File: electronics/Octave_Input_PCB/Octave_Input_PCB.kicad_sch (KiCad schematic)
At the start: 38 parts, among them SW1 SW_Hot_Swap_Socket, SW10 SW_Hot_Swap_Socket, SW11 SW_Hot_Swap_Socket, SW12 SW_Hot_Swap_Socket, SW13 SW_Hot_Swap_Socket, SW14 Alps_Alpine_RKJXV1224, SW15 Bourns_PEC12R-4xxxF-Sxxx, SW2 SW_Hot_Swap_Socket, SW3 SW_Hot_Swap_Socket, SW4 SW_Hot_Swap_Socket, SW5 SW_Hot_Swap_Socket, SW6 SW_Hot_Swap_Socket, SW7 SW_Hot_Swap_Socket, SW8 SW_Hot_Swap_Socket, SW9 SW_Hot_Swap_Socket, U1 Adafruit_QT_Py_RP2040, U2 Raspberry_Pi_RP2040

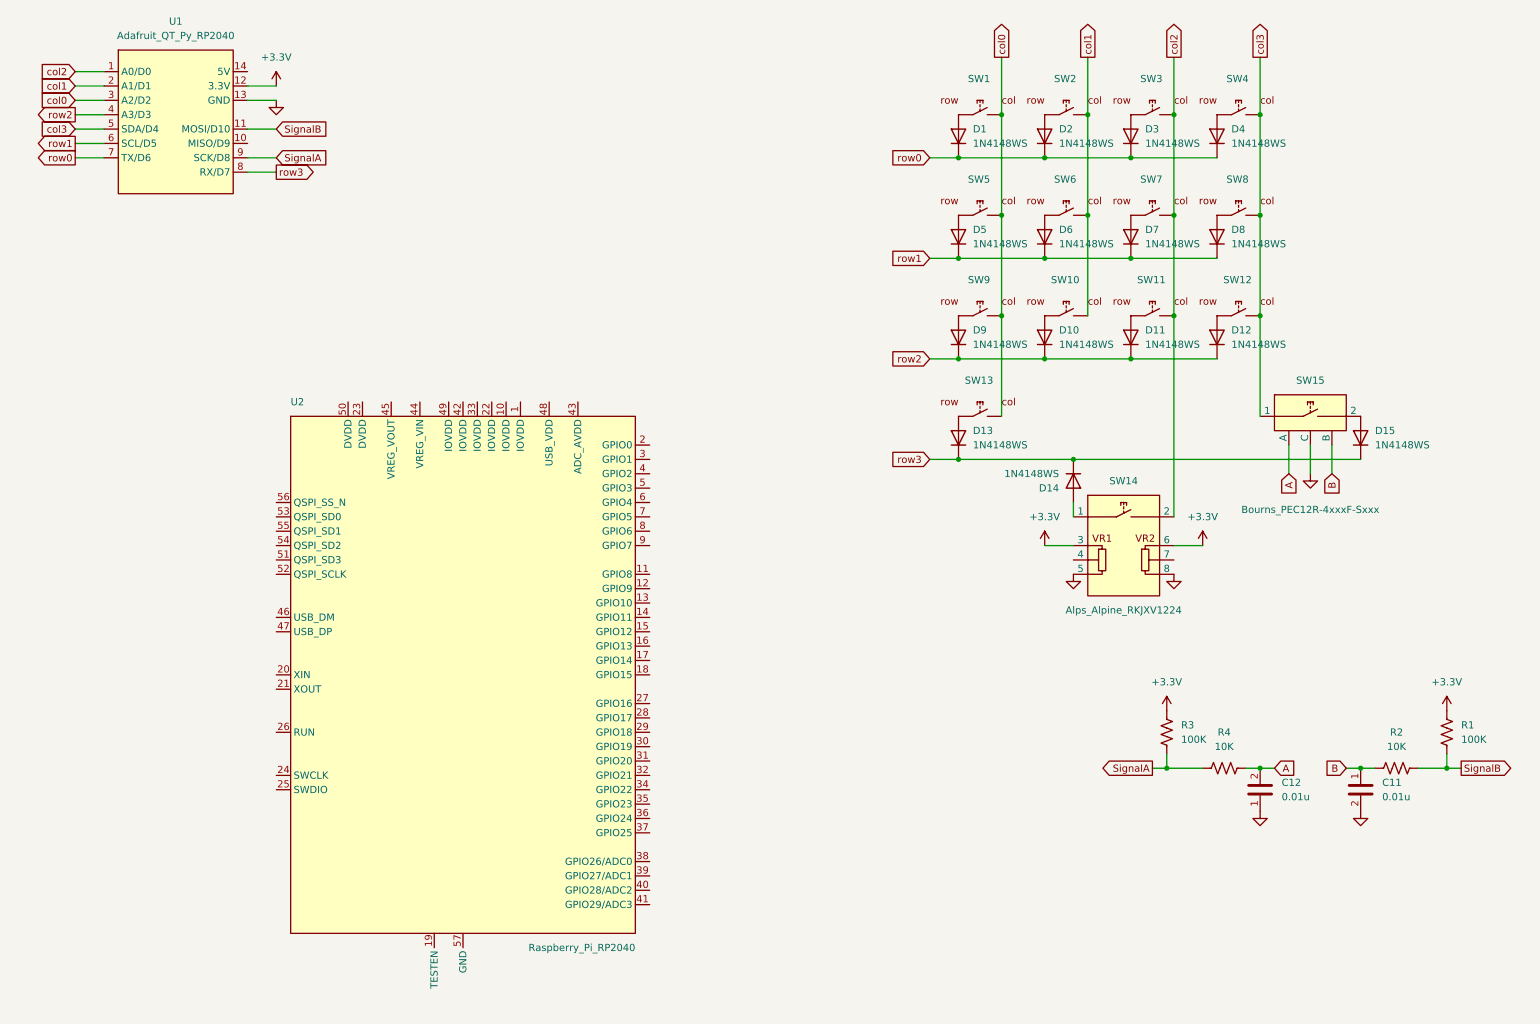
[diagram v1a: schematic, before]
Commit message: [WIP] Update schematic and PCB
Add a USB-C connector, but using the Molex 1054500101 makes routing very difficult.
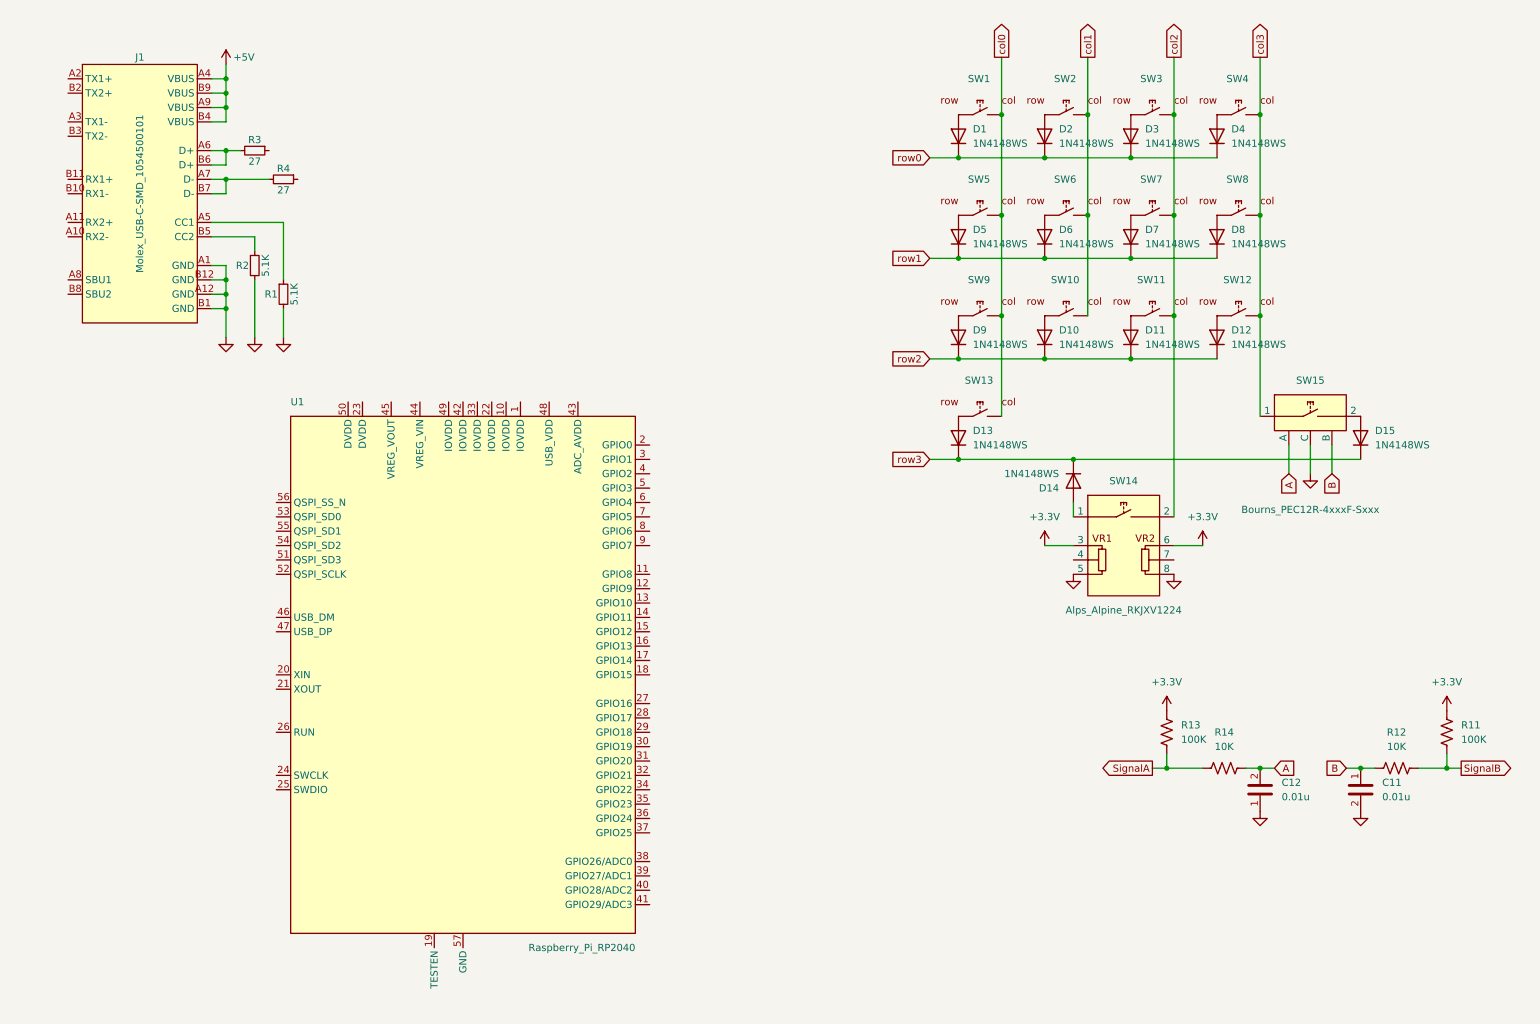
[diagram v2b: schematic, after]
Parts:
- removed U1: Adafruit_QT_Py_RP2040, Octave_Library:Adafruit_QT_Py_RP2040, symbol Octave_Library:Adafruit_QT_Py_RP2040
- added J1: Molex_USB-C-SMD_1054500101, Octave_Library:Molex_USB-C-SMD_1054500101, symbol Octave_Library:Molex_USB-C-SMD_1054500101
- added R1, R2: 5.1K, Resistor_SMD:R_0402_1005Metric, symbol Device:R_Small
- added R3, R4: 27, Resistor_SMD:R_0402_1005Metric, symbol Device:R_Small
- renumbered R1 to R11, R2 to R12, R3 to R13, R4 to R14, U2 to U1
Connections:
- net GND: now also J1.A1 (GND), J1.A12 (GND), J1.B1 (GND), J1.B12 (GND), R1.2, R2.2
- new net: J1.A6 (D+), J1.B6 (D+), R3.2
- new net: J1.A5 (CC1), R1.1
- new net: J1.A7 (D-), J1.B7 (D-), R4.2
- new net: J1.B5 (CC2), R2.1
- new net +5V: J1.A4 (VBUS), J1.A9 (VBUS), J1.B4 (VBUS), J1.B9 (VBUS)

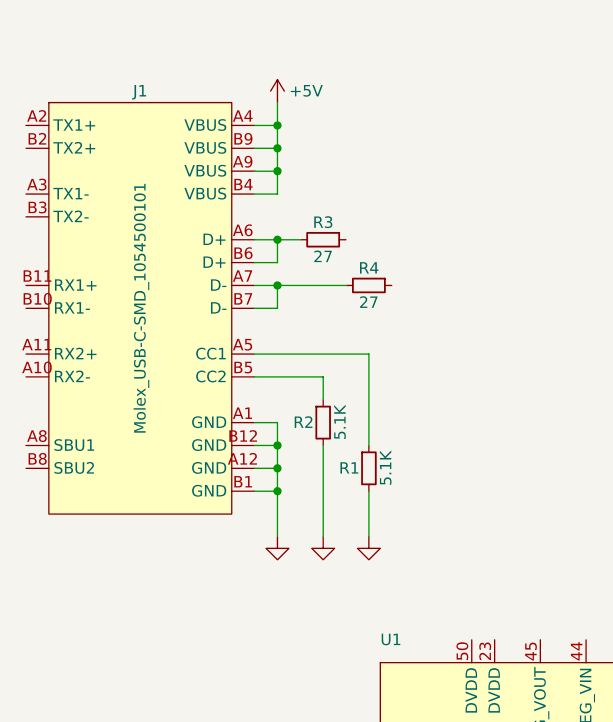
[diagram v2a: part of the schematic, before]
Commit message: Change the USB-C connector to HRO TYPE-C-31-M-12
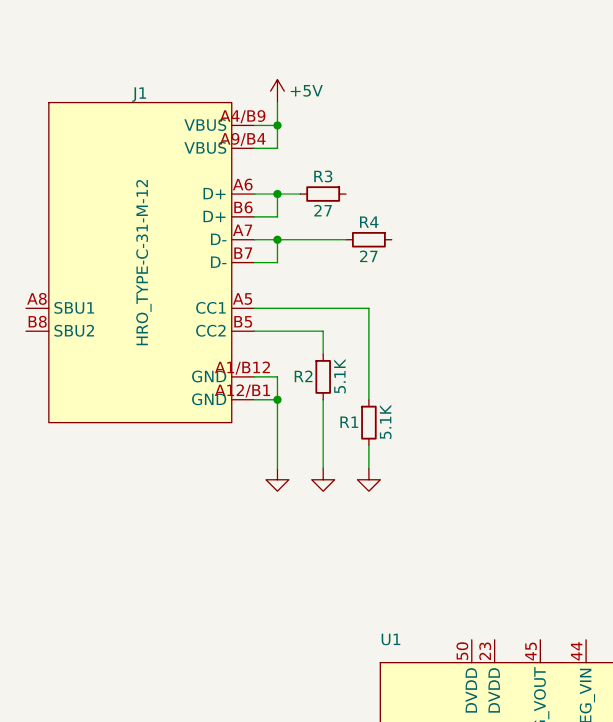
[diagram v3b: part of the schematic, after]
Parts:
- removed J1: Molex_USB-C-SMD_1054500101, Octave_Library:Molex_USB-C-SMD_1054500101, symbol Octave_Library:Molex_USB-C-SMD_1054500101
- added J1: HRO_TYPE-C-31-M-12, Octave_Library:HRO_TYPE-C-31-M-12, symbol Octave_Library:HRO_TYPE-C-31-M-12
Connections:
- net +5V: now also J1.A4/B9 (VBUS), J1.A9/B4 (VBUS)
- net GND: now also J1.A1/B12 (GND), J1.A12/B1 (GND)
- net at R3.2: now also J1.A6 (D+), J1.B6 (D+)
- net at R1.1: now also J1.A5 (CC1)
- net at R4.2: now also J1.A7 (D-), J1.B7 (D-)
- net at R2.1: now also J1.B5 (CC2)
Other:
- moved on the sheet: R1, R2, R3, R4

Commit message: [WIP] Update schematic and PCB
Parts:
- renumbered R2 to R1, R1 to R2
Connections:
- net D+: now reaches R3.1
- net D+: now also U1.47 (USB_DP)
- net D-: now reaches U1.46 (USB_DM)
- net D-: now also R4.1
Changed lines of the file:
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@@
   (title_block
     (title "Octave - Input PCB")
-    (date "2022-05-07")
+    (date "2022-05-08")
     (rev "5.a")
     (comment 4 "https://github.com/takayoshiotake/octave-12-key-macropad")
@@
     (stroke (width 0) (type default) (color 0 0 0 0))
   )
+  (wire (pts (xy 63.5 40.64) (xy 66.04 40.64))
+    (stroke (width 0) (type default) (color 0 0 0 0))
+  )
   (wire (pts (xy 50.8 43.18) (xy 50.8 40.64))
     (stroke (width 0) (type default) (color 0 0 0 0))
@@
   )
   (wire (pts (xy 180.34 77.47) (xy 195.58 77.47))
+    (stroke (width 0) (type default) (color 0 0 0 0))
+  )
+  (wire (pts (xy 58.42 35.56) (xy 66.04 35.56))
     (stroke (width 0) (type default) (color 0 0 0 0))
   )
@@
     )
   )
+  (global_label "D+" (shape input) (at 59.69 125.73 180) (fields_autoplaced)
+    (effects (font (size 1.27 1.27)) (justify right))
+    (property "Intersheet References" "${INTERSHEET_REFS}" (id 0) (at 54.4345 125.6506 0)
+      (effects (font (size 1.27 1.27)) (justify right) hide)
+    )
+  )
   (global_label "col2" (shape output) (at 218.44 24.13 90) (fields_autoplaced)
     (effects (font (size 1.27 1.27)) (justify left))
@@
     )
   )
+  (global_label "D+" (shape input) (at 66.04 35.56 0) (fields_autoplaced)
+    (effects (font (size 1.27 1.27)) (justify left))
+    (property "Intersheet References" "${INTERSHEET_REFS}" (id 0) (at 71.2955 35.4806 0)
+      (effects (font (size 1.27 1.27)) (justify left) hide)
+    )
+  )
   (global_label "col1" (shape output) (at 203.2 24.13 90) (fields_autoplaced)
     (effects (font (size 1.27 1.27)) (justify left))
@@
     )
   )
+  (global_label "D-" (shape input) (at 66.04 40.64 0) (fields_autoplaced)
+    (effects (font (size 1.27 1.27)) (justify left))
+    (property "Intersheet References" "${INTERSHEET_REFS}" (id 0) (at 71.2955 40.5606 0)
+      (effects (font (size 1.27 1.27)) (justify left) hide)
+    )
+  )
   (global_label "SignalB" (shape output) (at 269.24 149.86 0) (fields_autoplaced)
     (effects (font (size 1.27 1.27)) (justify left))
     (property "Intersheet References" "${INTERSHEET_REFS}" (id 0) (at 278.8498 149.7806 0)
       (effects (font (size 1.27 1.27)) (justify left) hide)
+    )
+  )
+  (global_label "D-" (shape input) (at 59.69 123.19 180) (fields_autoplaced)
+    (effects (font (size 1.27 1.27)) (justify right))
+    (property "Intersheet References" "${INTERSHEET_REFS}" (id 0) (at 54.4345 123.1106 0)
+      (effects (font (size 1.27 1.27)) (justify right) hide)
     )
   )
@@
   (symbol (lib_id "Device:R_Small") (at 60.96 60.96 0) (unit 1)
     (in_bom yes) (on_board yes)
-    (property "Reference" "R1" (id 0) (at 59.944 60.96 0)
+    (property "Reference" "R2" (id 0) (at 59.944 60.96 0)
       (effects (font (size 1.27 1.27)) (justify right))
     )
@@
   (symbol (lib_id "Device:R_Small") (at 55.88 55.88 0) (unit 1)
     (in_bom yes) (on_board yes)
-    (property "Reference" "R2" (id 0) (at 54.864 55.88 0)
+    (property "Reference" "R1" (id 0) (at 54.864 55.88 0)
       (effects (font (size 1.27 1.27)) (justify right))
     )
@@
       (reference "J1") (unit 1) (value "HRO_TYPE-C-31-M-12") (footprint "Octave_Library:HRO_TYPE-C-31-M-12")
     )
+    (path "/575bc9c1-f53b-4dee-b3d5-6bbc484509fa"
+      (reference "R1") (unit 1) (value "5.1K") (footprint "Resistor_SMD:R_0402_1005Metric")
+    )
     (path "/46e29ce0-dad0-48cf-b29f-d5905871cde0"
-      (reference "R1") (unit 1) (value "5.1K") (footprint "Resistor_SMD:R_0402_1005Metric")
-    )
-    (path "/575bc9c1-f53b-4dee-b3d5-6bbc484509fa"
       (reference "R2") (unit 1) (value "5.1K") (footprint "Resistor_SMD:R_0402_1005Metric")
     )

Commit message: [WIP] Update schematic and PCB
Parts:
- added C1, C13, C14, C2, C3, C4: 1uF, Capacitor_SMD:C_0402_1005Metric, symbol Device:C_Small
- added C10, C11, C12, C5, C6, C7, C8, C9: 0.1uF, Capacitor_SMD:C_0402_1005Metric, symbol Device:C_Small
- added U1: AP2112K-3.3, Package_TO_SOT_SMD:SOT-23-5, symbol Regulator_Linear:AP2112K-3.3
- renumbered C11 to C21, C12 to C22, U1 to U2
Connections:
- net +3V3: now also U2.1 (IOVDD), U2.10 (IOVDD), U2.22 (IOVDD), U2.33 (IOVDD), U2.42 (IOVDD), U2.43 (ADC_AVDD), U2.44 (VREG_VIN), U2.48 (USB_VDD), U2.49 (IOVDD), C10.1, C13.1, C14.1, C2.1, C3.1, C5.1, C6.1, C7.1, C8.1, C9.1, U1.5 (VOUT)
- net +5V: now also C1.1, U1.1 (VIN), U1.3 (EN)
- net GND: now also U2.19 (TESTEN), U2.57 (GND), C1.2, C10.2, C11.2, C12.2, C13.2, C14.2, C2.2, C3.2, C4.2, C5.2, C6.2, C7.2, C8.2, C9.2, U1.2 (GND)
- net +1V1: now reaches U2.23 (DVDD)
- net +1V1: now also U2.45 (VREG_VOUT), U2.50 (DVDD), C11.1, C12.1, C4.1
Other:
- note added: "Close to ADC_AVDD"
- note added: "Close to USB_VDD"
- note added: "Close to VREG_VIN"
- note added: "Close to VREG_VOUT"
- note added: "Close to each DVDD"
- note added: "Close to each IOVDD"
- note added: "Make sure R3 and R4 are close to RP2040"
- moved on the sheet: D1, D10, D11, D12, D13, D14, D15, D2, D3, D4, D5, D6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

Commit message: [WIP] Update schematic and PCB
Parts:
- added U3: W25Q64JVSS, Package_SO:SOIC-8_5.23x5.23mm_P1.27mm, symbol Memory_Flash:W25Q32JVSS
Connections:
- net +3V3: now also U3.8 (VCC)
- net GND: now also U3.4 (GND)
- net QSPI_SD3: now reaches U2.51 (QSPI_SD3)
- net QSPI_SD3: now also U3.7 (IO3)
- net QSPI_SCLK: now reaches U2.52 (QSPI_SCLK)
- net QSPI_SCLK: now also U3.6 (CLK)
- net QSPI_SD0: now reaches U2.53 (QSPI_SD0)
- net QSPI_SD0: now also U3.5 (DI(IO0))
- net QSPI_SD2: now reaches U2.54 (QSPI_SD2)
- net QSPI_SD2: now also U3.3 (IO2)
- net QSPI_SD1: now reaches U2.55 (QSPI_SD1)
- net QSPI_SD1: now also U3.2 (DO(IO1))
- net QSPI_SS_N: now reaches U2.56 (QSPI_SS_N)
- net QSPI_SS_N: now also U3.1 (~{CS})
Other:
- moved on the sheet: C10, C11, C12, C13, C14, C3, C4, C5, C6, C7, C8, C9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
